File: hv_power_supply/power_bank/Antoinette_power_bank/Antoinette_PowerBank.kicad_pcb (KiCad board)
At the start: 2 copper layers, 86.4 x 53.3 mm, 43 parts, among them J1 NanoFit_RA_TH_02, J2 USB-Micro-1981568-1, J3 NanoFit_RA_TH_02, J4 USB-A-S-X-X-SM2, Q1 SSM3K333R, U2 MCP73871T-2CCI_ML, U3 TPS61090RSAR

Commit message: made sure to connect all pins
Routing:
- net VBUS: track 34.0 -> 41.7 mm, vias 2 -> 3
- net GND: track 73.0 -> 74.7 mm
- net /Battery+: track 17.4 -> 17.9 mm

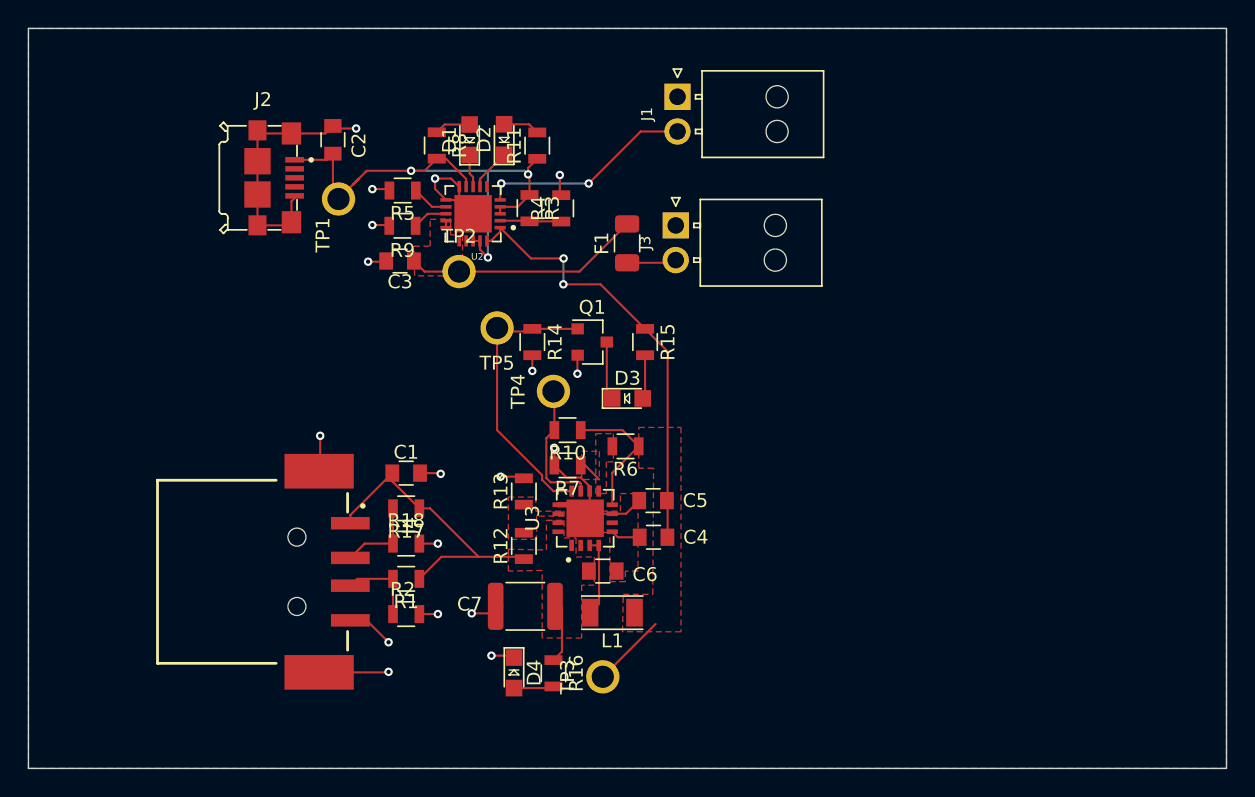
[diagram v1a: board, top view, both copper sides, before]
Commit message: put tp farther from components, used more copper pours, and put vias closer together
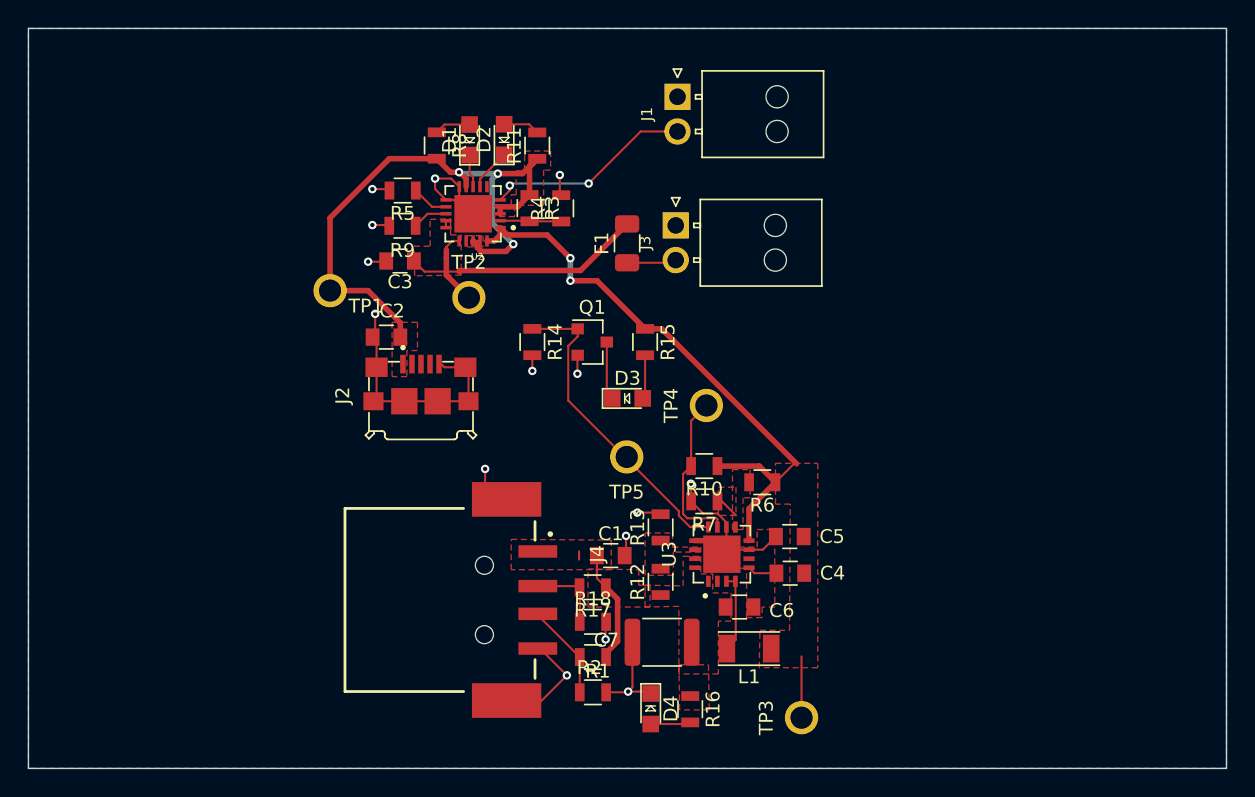
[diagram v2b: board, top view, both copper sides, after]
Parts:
- moved J2 20.0 mm to (79.1, 52.3), turned to 0 degrees
- moved C1 15.9 mm to (92.8, 63.4)
- moved C2 14.7 mm to (76.6, 47.7), turned to 180 degrees
- moved TP3 14.6 mm to (106.5, 75.1)
- moved R17 14.6 mm to (91.5, 65.7)
- moved R1 14.6 mm to (91.5, 70.7)
- moved R2 14.6 mm to (91.5, 73.3)
- moved R18 14.6 mm to (91.5, 68.2)
- moved J4 13.7 mm to (83.7, 66.6)
- moved TP5 13.2 mm to (93.9, 56.3)
- moved TP4 11.1 mm to (99.7, 52.6)
- moved C5 10.2 mm to (105.7, 62.0)
- moved D4 10.2 mm to (95.7, 74.4)
- moved C4 10.2 mm to (105.7, 64.7)
- moved C6 10.2 mm to (102.1, 67.1)
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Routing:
- net +5V: track 26.7 -> 10.7 mm
- net VBUS: track 41.7 -> 48.0 mm
- net /Battery+: track 17.9 -> 24.0 mm
- net GND: track 74.7 -> 77.6 mm, vias 18 -> 15
- net Net-(Q1-Pad1): track 20.6 -> 23.3 mm
- net Net-(R10-Pad2): track 10.0 -> 12.0 mm
- net Net-(J4-Pad03): track 6.52 -> 7.61 mm
- net /16KThermistor: track 15.6 -> 15.0 mm
- added copper zone on F.Cu, net VBUS

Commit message: modify schematic to be pull up resistor for LBO pin and update PCB layout to fit DXF
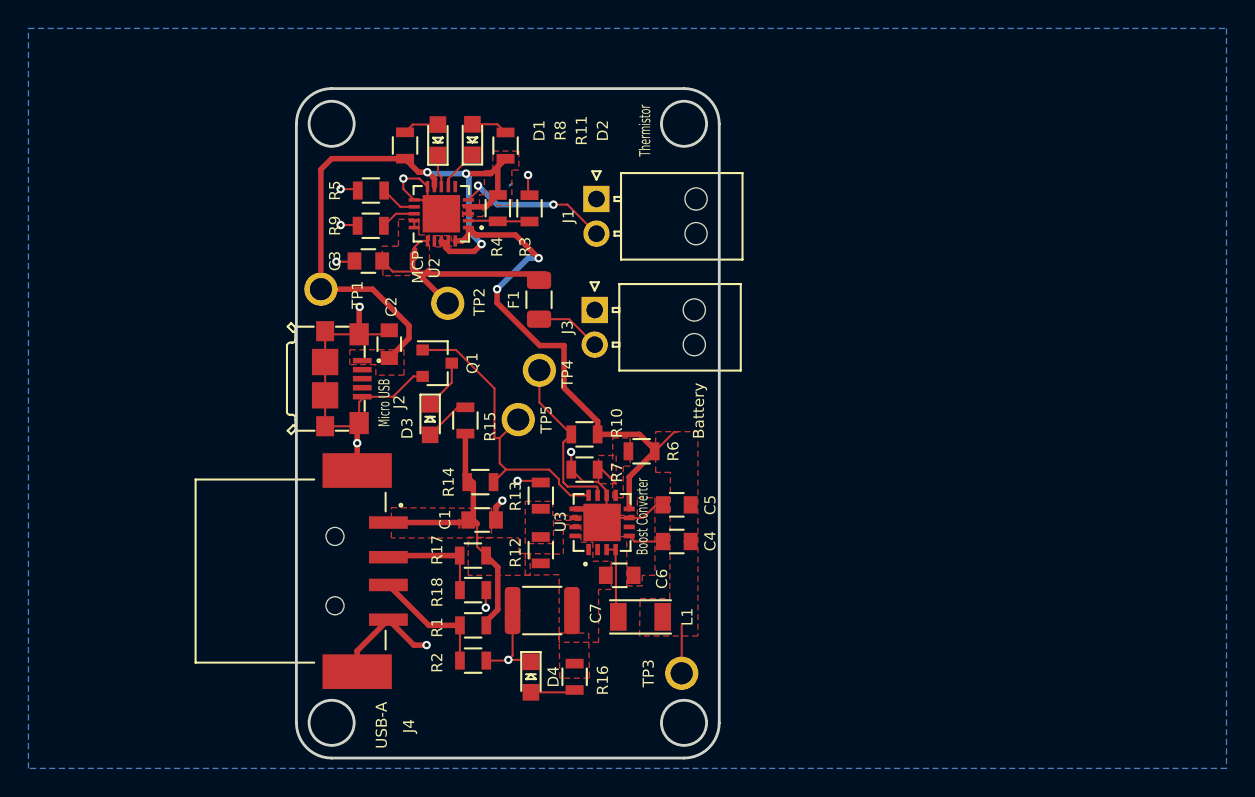
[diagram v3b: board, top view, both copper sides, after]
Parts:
- moved D3 14.3 mm to (79.8, 53.6), turned to 270 degrees
- moved R15 14.1 mm to (82.3, 53.7), turned to 90 degrees
- moved TP4 12.3 mm to (87.6, 50.0)
- moved Q1 11.3 mm to (80.3, 49.5)
- moved J4 11.0 mm to (72.9, 64.5)
- moved R14 10.8 mm to (83.4, 58.1), turned to 0 degrees
- moved C1 9.62 mm to (83.5, 60.8)
- moved J1 9.40 mm to (91.7, 37.7)
- moved TP3 9.21 mm to (97.9, 71.9)
- moved R6 8.98 mm to (95.0, 55.9)
- moved D4 8.93 mm to (87.0, 72.2)
- moved C6 8.93 mm to (93.4, 64.8)
- moved C7 8.93 mm to (87.8, 67.4)
- moved R1 8.93 mm to (82.9, 68.4)
- moved R10 8.93 mm to (90.9, 54.7)
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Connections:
- R14 pad 1: Net-(Q1-Pad1) -> +5V
- R14 pad 2: GND -> Net-(Q1-Pad1)
- R15 pad 1: +BATT -> +5V
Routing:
- net +5V: track 10.7 -> 24.0 mm
- net +BATT: track 47.1 -> 42.3 mm
- net /16KThermistor: track 15.0 -> 11.3 mm
- net /Battery+: track 24.0 -> 20.4 mm
- net VBUS: track 48.0 -> 51.3 mm
- net Net-(J4-Pad02): track 5.58 -> 7.85 mm
- net GND: track 77.6 -> 79.7 mm, vias 15 -> 13
- net Net-(F1-Pad1): track 5.34 -> 6.80 mm
- net Net-(J4-Pad03): track 7.61 -> 8.90 mm
- net Net-(L1-Pad2): track 5.84 -> 4.93 mm
- net Net-(R10-Pad2): track 12.0 -> 12.8 mm
- net Net-(D3-Pad1): track 4.23 -> 3.61 mm
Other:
- board size 86.4 x 53.3 mm -> 30.5 x 48.3 mm
- board text added: "Battery"
- board text added: "Boost Converter"
- board text added: "MCP"
- board text added: "Micro USB"
- board text added: "Thermistor"
- board text added: "USB-A"

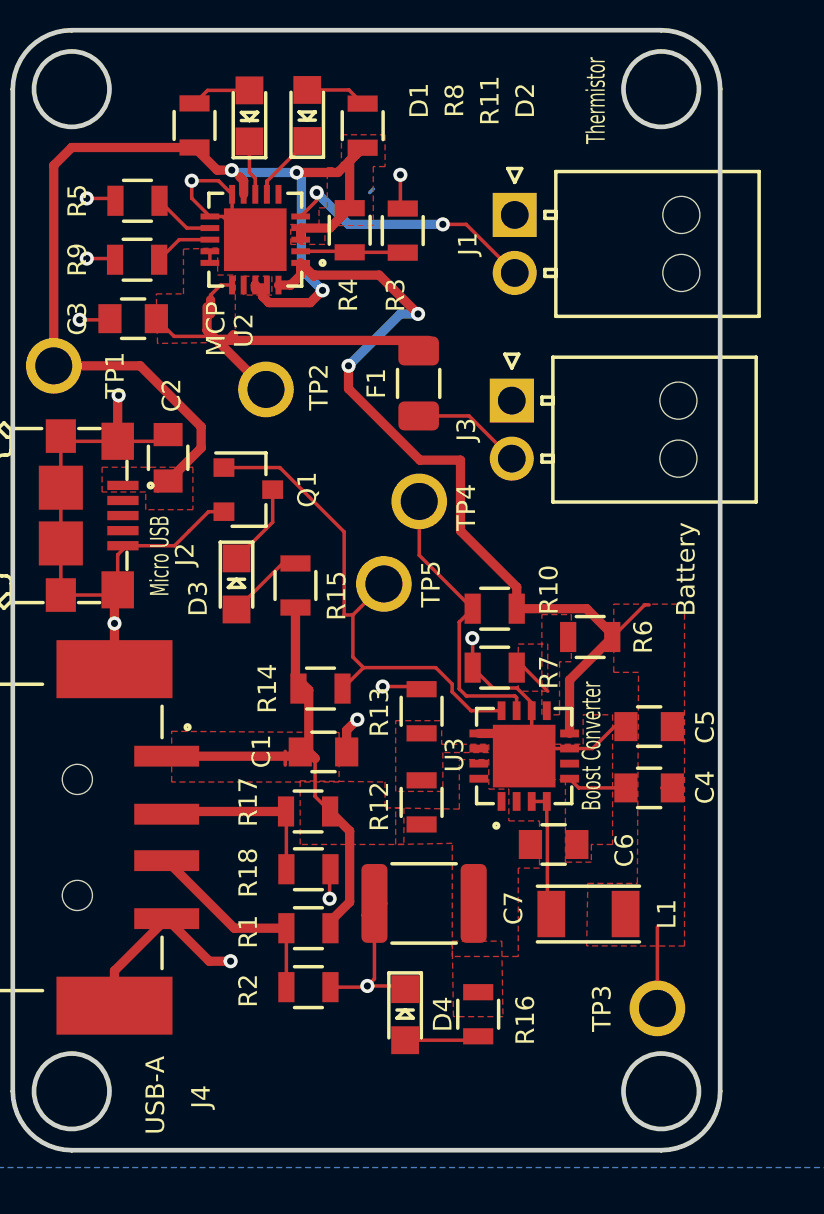
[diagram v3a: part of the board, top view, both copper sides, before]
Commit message: cleaned traces, shortened vias, spaced tp
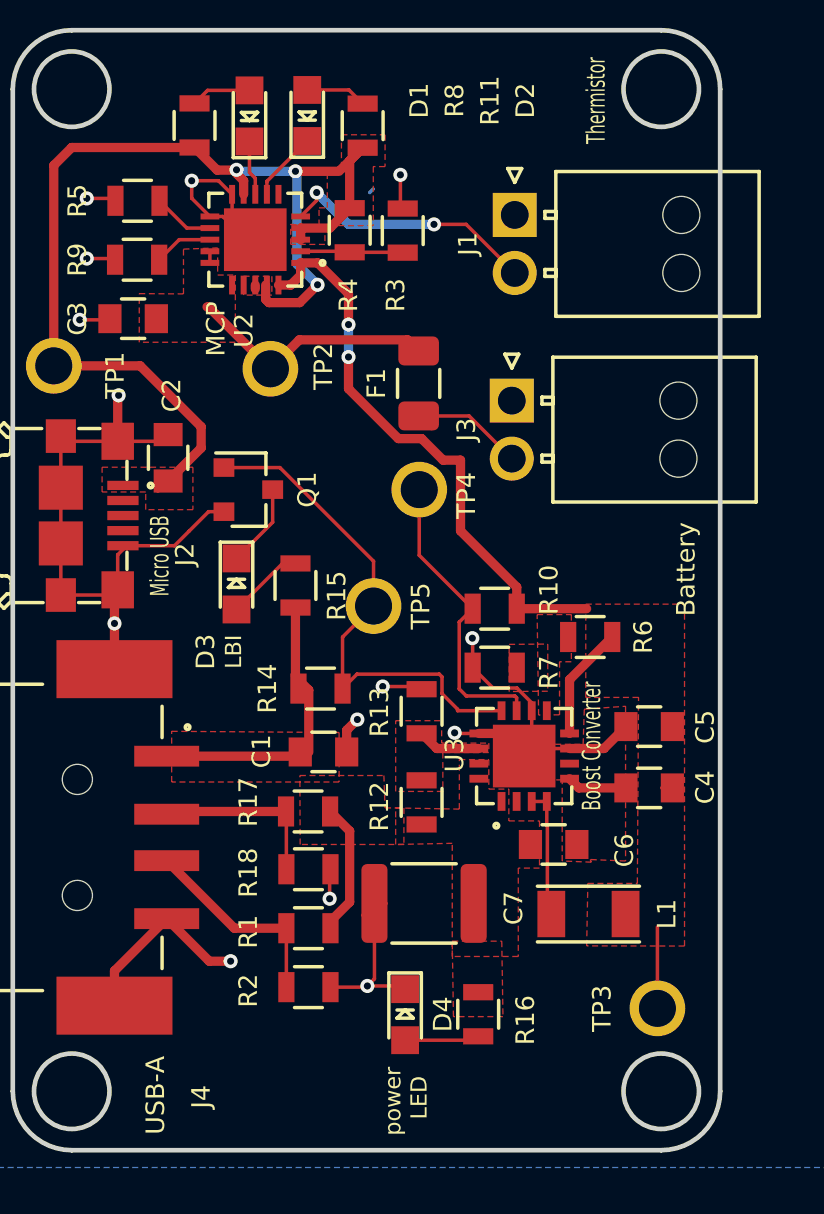
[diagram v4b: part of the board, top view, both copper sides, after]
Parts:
- moved TP5 1.05 mm to (85.7, 54.5)
- moved TP2 0.91 mm to (81.2, 44.3)
- moved TP4 0.51 mm to (87.6, 49.5)
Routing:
- net /Battery+: track 20.4 -> 12.2 mm
- net +BATT: track 42.3 -> 34.1 mm
- net +5V: track 24.0 -> 19.9 mm
- net Net-(R12-Pad2): track 0.00 -> 2.74 mm
- net GND: track 79.7 -> 81.7 mm, vias 13 -> 14
- net Net-(R6-Pad2): track 1.76 -> 0.00 mm
- net VBUS: track 51.3 -> 49.7 mm
- net Net-(D2-Pad1): track 4.05 -> 3.02 mm
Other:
- board text added: "LBI"
- board text added: "power LED"

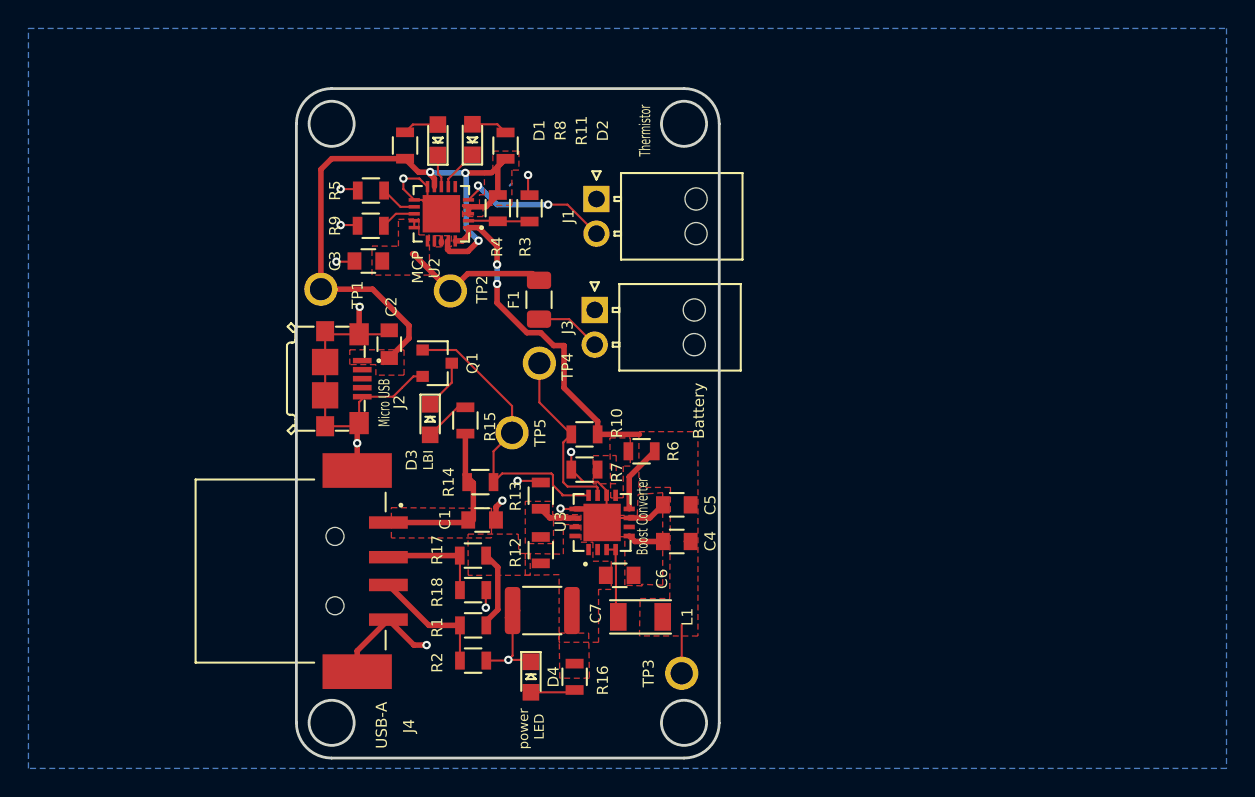
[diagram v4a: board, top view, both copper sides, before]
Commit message: Add switch and cleaned up board
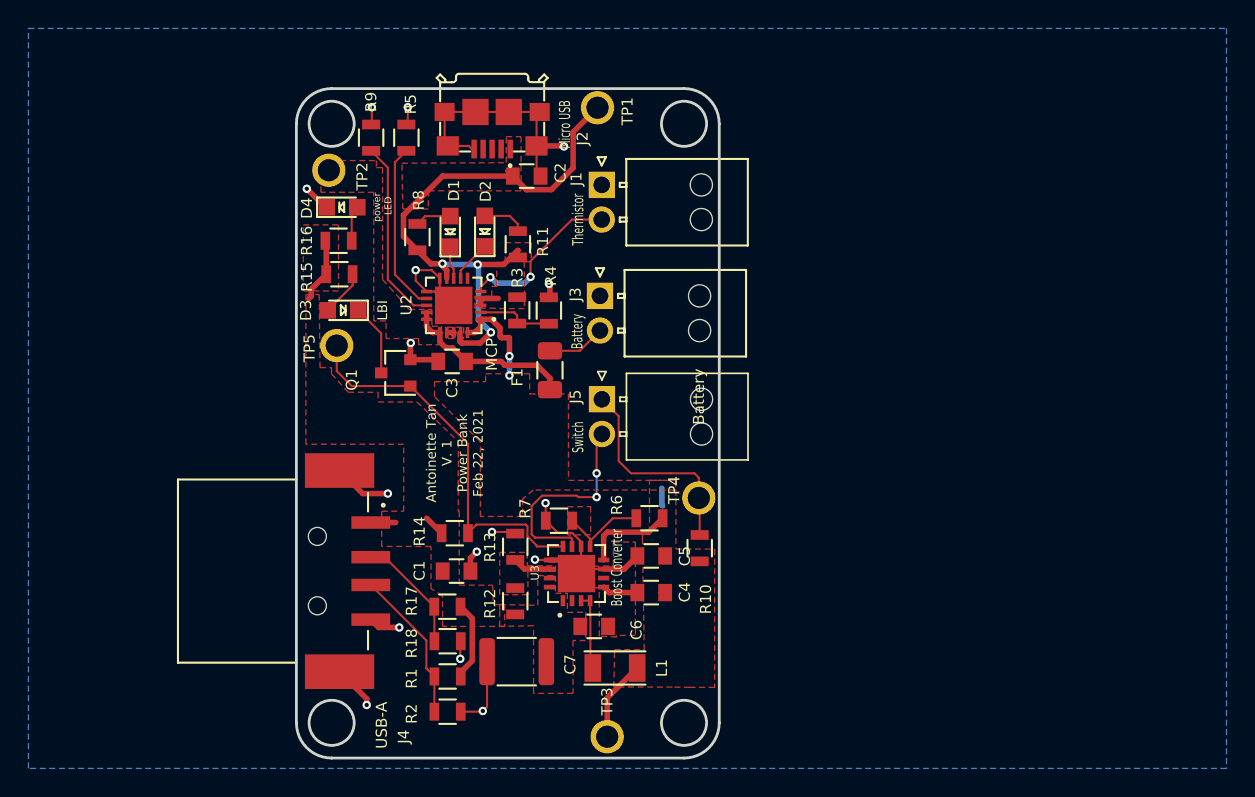
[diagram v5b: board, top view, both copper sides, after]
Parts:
- added J5: NanoFit_RA_TH_02, Formula:NanoFit_Molex_1x02x2.50mm_Angled_OEM, F.Cu at (92.1, 52.1)
- moved D4 36.5 mm to (73.4, 38.3), turned to 0 degrees
- moved R16 35.7 mm to (73.2, 40.7), turned to 0 degrees
- moved TP1 23.8 mm to (91.8, 31.1), turned to 270 degrees
- moved J2 22.7 mm to (84.2, 31.4), turned to 180 degrees
- moved C2 15.6 mm to (86.7, 36.0), turned to 0 degrees
- moved TP4 15.0 mm to (99.1, 59.2)
- moved TP5 14.1 mm to (73.0, 48.3)
- moved R15 13.9 mm to (73.2, 43.1), turned to 0 degrees
- moved TP2 12.3 mm to (72.5, 35.6)
- moved R10 11.7 mm to (99.2, 62.9), turned to 90 degrees
- moved D3 10.1 mm to (73.5, 45.7), turned to 180 degrees
- moved C3 9.43 mm to (81.3, 49.4)
- moved R3 7.50 mm to (86.0, 45.7)
- moved R4 7.50 mm to (88.3, 45.7)
- moved R11 7.17 mm to (86.1, 41.0)
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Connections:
- R10 pad 2: Net-(R10-Pad2) -> Net-(J5-Pad1)
- TP4 pad 1: Net-(R10-Pad2) -> Net-(J5-Pad1)
- U3 pad 11: Net-(R10-Pad2) -> /switch
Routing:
- net Net-(J5-Pad1): track 0.00 -> 15.6 mm
- net /switch: track 0.00 -> 15.4 mm, vias 0 -> 2
- net +BATT: track 34.1 -> 20.9 mm
- net Net-(R10-Pad2): track 12.8 -> 0.00 mm
- net Net-(R9-Pad1): track 2.54 -> 13.3 mm
- net Net-(R5-Pad1): track 2.66 -> 12.3 mm
- net Net-(R6-Pad2): track 0.00 -> 6.79 mm
- net Net-(Q1-Pad1): track 22.4 -> 28.1 mm
- net GND: track 81.7 -> 76.2 mm, vias 14 -> 16
- net VBUS: track 49.7 -> 44.4 mm
- net +5V: track 19.9 -> 15.9 mm
- net Net-(J4-Pad03): track 8.90 -> 11.3 mm
- net Net-(D3-Pad1): track 3.61 -> 5.20 mm
- net Net-(J4-Pad02): track 7.85 -> 9.27 mm
- net Net-(F1-Pad1): track 6.80 -> 5.46 mm
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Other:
- board text added: "Antoinette Tan V. 1 Power Bank Feb 22, 2021"
- board text added: "Switch"
